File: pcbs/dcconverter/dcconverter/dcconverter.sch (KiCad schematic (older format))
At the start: 22 parts, among them IC1 NCP7805TG, J1 190-9991, J2 897-0711, J3 146-8335, Q1 124-8981, Q2 FQP47P06, Q3 2SK3747-1E

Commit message: Finish Schematic for PCB
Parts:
- removed Q3: 2SK3747-1E, TO545P570X1550X2990-3P, symbol SamacSys_Parts:2SK3747-1E
- added C4: 711-2096, Capacitor_THT:C_Disc_D7.5mm_W5.0mm_P7.50mm, symbol Device:C
- added D3, D4: 800-8872, Diode_THT:D_DO-41_SOD81_P10.16mm_Horizontal, symbol Device:D_Zener
- added HS-IC1: 893-4942, Heatsink:Heatsink_Fischer_SK129-STS_42x25mm_2xDrill2.5mm, symbol Mechanical:Heatsink_Pad_2Pin
- added Q10, Q5, Q6: 398-433, Package_TO_SOT_THT:TO-92_Inline, symbol Transistor_BJT:2N2219
- added Q3, Q4: 2SK3747-1E, Package_TO_SOT_THT:TO-3P-3_Horizontal_TabDown, symbol Transistor_FET:2N7000
- added Q7: 671-5118, Package_TO_SOT_THT:TO-220-3_Horizontal_TabDown, symbol Transistor_FET:AO3401A
- added Q8: 671-4809, Package_TO_SOT_THT:TO-3P-3_Horizontal_TabDown, symbol Transistor_FET:2N7000
- added R10: 10k, Resistor_THT:R_Axial_DIN0207_L6.3mm_D2.5mm_P10.16mm_Horizontal, symbol Device:R
- added R11, R7, R8: 220, Resistor_THT:R_Axial_DIN0207_L6.3mm_D2.5mm_P10.16mm_Horizontal, symbol Device:R
- added R5: 10M, Resistor_THT:R_Axial_DIN0207_L6.3mm_D2.5mm_P10.16mm_Horizontal, symbol Device:R
- added R6: 707-8546, Resistor_THT:R_Axial_DIN0207_L6.3mm_D2.5mm_P10.16mm_Horizontal, symbol Device:R
- added R9: 1k, Resistor_THT:R_Axial_DIN0207_L6.3mm_D2.5mm_P10.16mm_Horizontal, symbol Device:R
- IC1: footprint TO254P482X997X2018-3P -> Package_TO_SOT_THT:TO-220-3_Vertical
- J2: value 897-0711 -> 766-6629; footprint TerminalBlock_Altech:Altech_AK300_1x06_P5.00mm_45-Degree -> SamacSys_Parts:CES-106-XX-Y-S
- Q1: value 124-8981 -> NGTB40N120FL2WG
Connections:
- net at C1.2, C2.2, C3.2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: now also C4.2, D4.2 (A), Q10.1 (E), Q6.1 (E), Q8.1 (S)
- net at F1.1, Q1.1 (C), R3.1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: now also R5.1, R6.1
- net at Q1.3 (G): now also Q7.3 (D), Q8.3 (D)
- net at C2.1, R1.2, R2.1: now also J2.3 (Pin_3); no longer J2.2 (Pin_2)
- net at IC1.3 (OUTPUT): now also J2.2 (Pin_2); no longer J2.3 (Pin_3)
- net at J2.4 (Pin_4): now also R7.2
- net at J2.5 (Pin_5): now also R8.2
- net at J2.6 (Pin_6): now also R11.2
- net at D2.1 (K), R3.2: now also Q3.2 (G)
- net at R4.2: now also Q3.3 (D)
- net at C3.1, IC1.1 (INPUT): now also Q3.1 (S), R10.1
- net at Q2.1: now also Q10.3 (C), R10.2
- new net: D3.1 (K), Q4.2 (G), R5.2
- new net: Q4.3 (D), R6.2
- new net: D3.2 (A), D4.1 (K)
- new net: C4.1, Q4.1 (S), Q7.2 (S), R9.1
- new net: Q5.2 (B), R7.1
- new net: Q6.2 (B), R8.1
- new net: Q5.1 (E), Q6.3 (C)
- new net: Q5.3 (C), Q7.1 (G), Q8.2 (G), R9.2
- new net: Q10.2 (B), R11.1

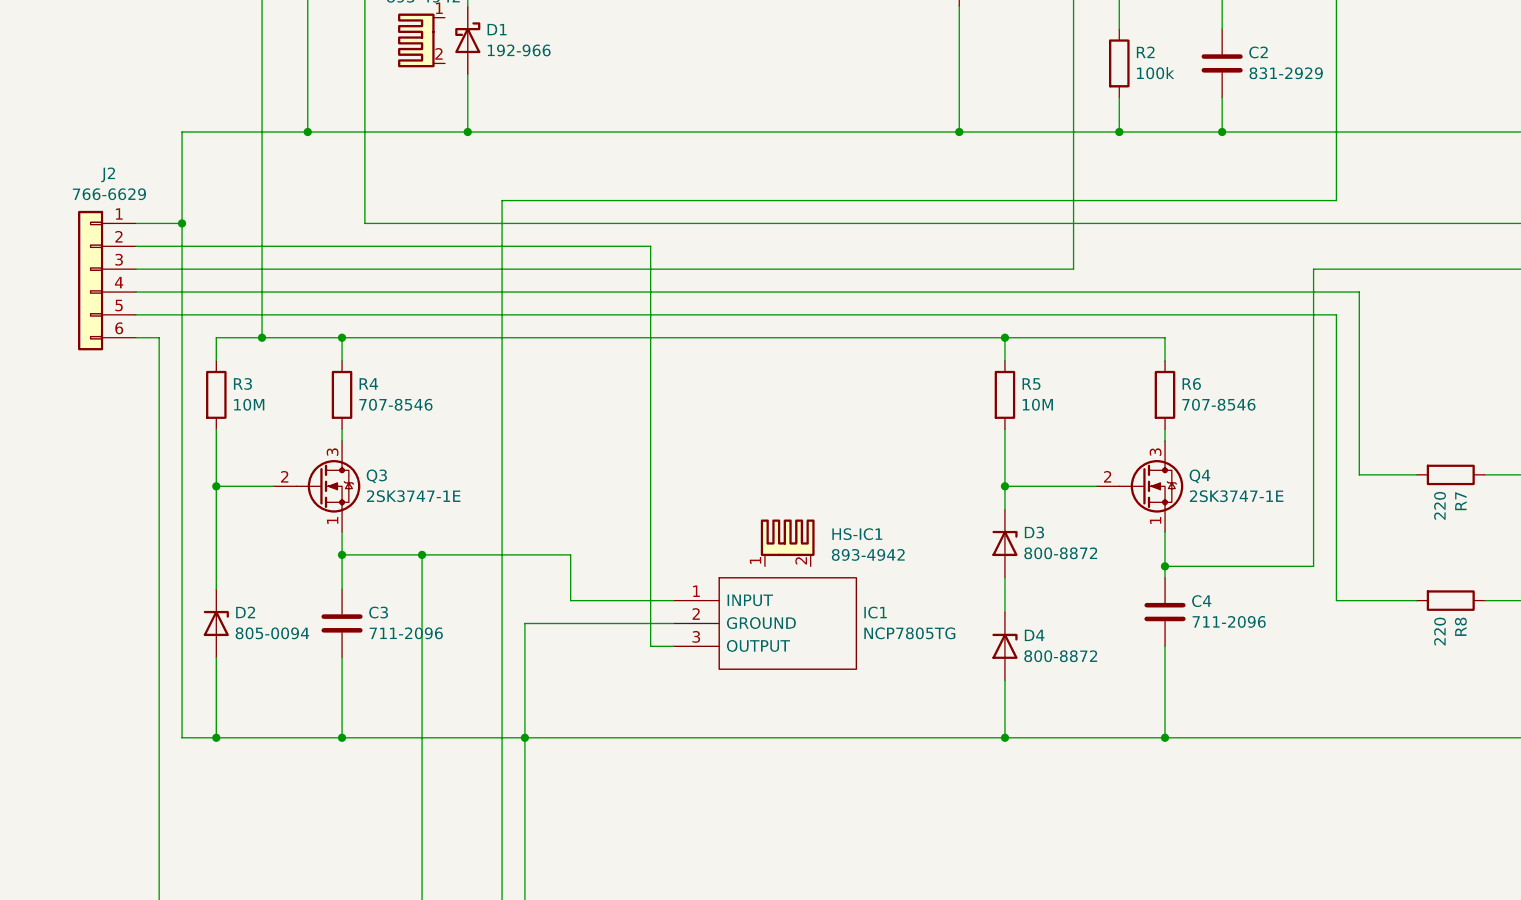
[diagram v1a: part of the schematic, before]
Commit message: Start with routing of DC Converter
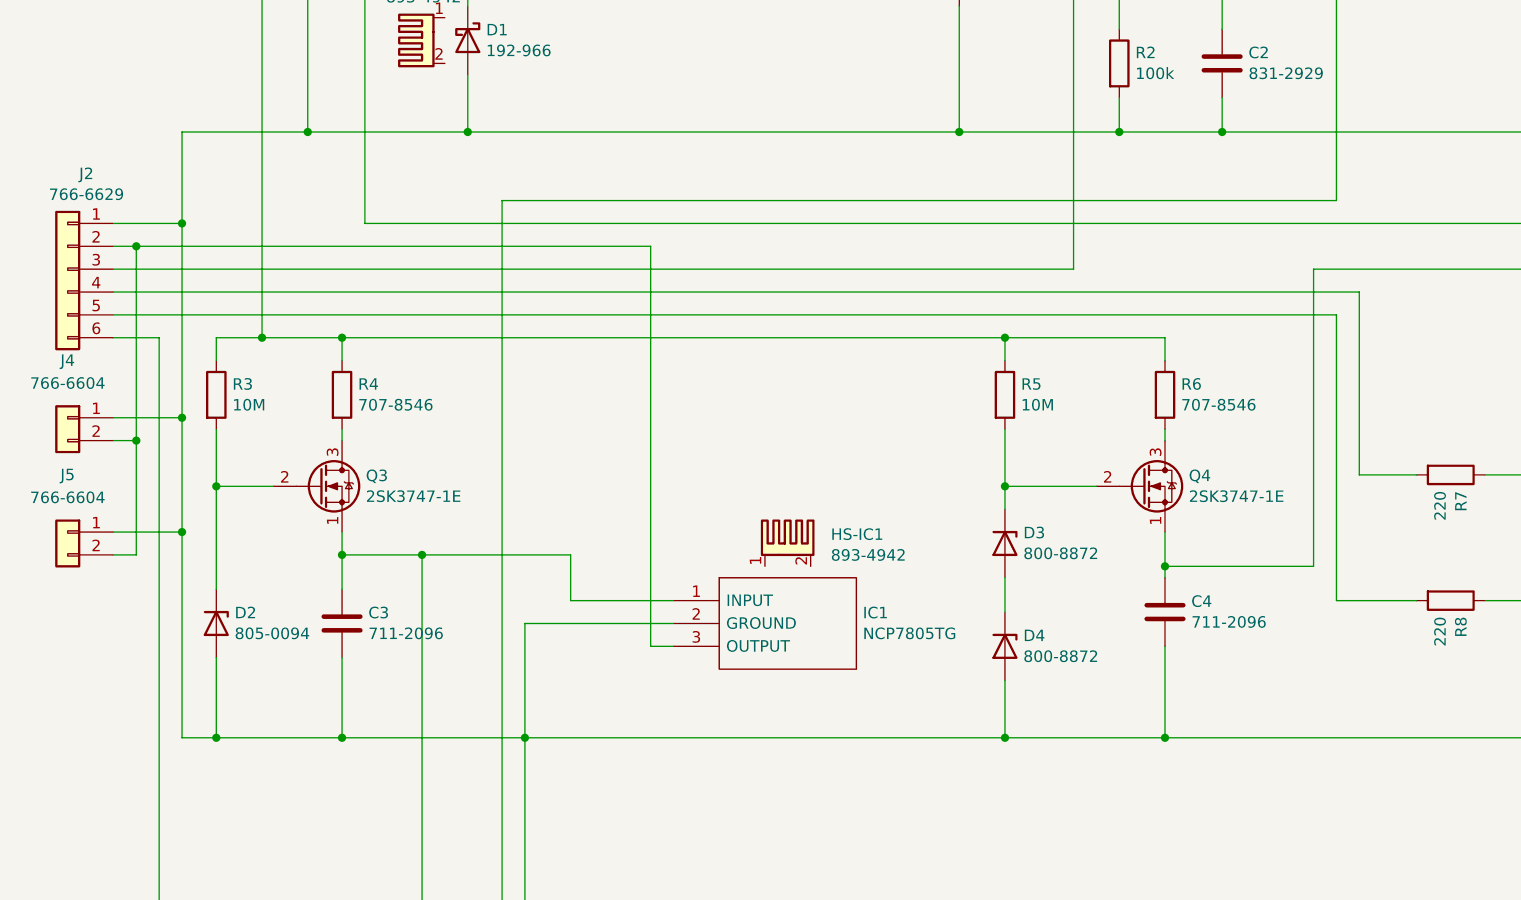
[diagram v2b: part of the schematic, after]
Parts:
- added J4, J5: 766-6604, SamacSys_Parts:CES-102-XX-Y-S, symbol Connector_Generic:Conn_01x02
- C3, C4: footprint Capacitor_THT:C_Disc_D7.5mm_W5.0mm_P7.50mm -> Capacitor_THT:CP_Radial_D18.0mm_P7.50mm
- Q8: footprint Package_TO_SOT_THT:TO-3P-3_Horizontal_TabDown -> Package_TO_SOT_THT:TO-220-3_Horizontal_TabDown
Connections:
- net at C1.2, C2.2, C3.2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: now also J4.1 (Pin_1), J5.1 (Pin_1)
- net at IC1.3 (OUTPUT), J2.2 (Pin_2): now also J4.2 (Pin_2), J5.2 (Pin_2)
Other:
- moved on the sheet: J2
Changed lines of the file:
@@
 L Connector_Generic:Conn_01x06 J2
 U 1 1 5F93B3A3
-P 1250 3700
-F 0 "J2" H 1168 4117 50  0000 C CNN
-F 1 "766-6629" H 1168 4026 50  0000 C CNN
-F 2 "SamacSys_Parts:CES-106-XX-Y-S" H 1250 3700 50  0001 C CNN
-F 3 "~" H 1250 3700 50  0001 C CNN
-	1    1250 3700
+P 1150 3700
+F 0 "J2" H 1068 4117 50  0000 C CNN
+F 1 "766-6629" H 1068 4026 50  0000 C CNN
+F 2 "SamacSys_Parts:CES-106-XX-Y-S" H 1150 3700 50  0001 C CNN
+F 3 "~" H 1150 3700 50  0001 C CNN
+	1    1150 3700
 	-1   0    0    -1
 $EndComp
@@
 F 0 "C3" H 2465 5296 50  0000 L CNN
 F 1 "711-2096" H 2465 5205 50  0000 L CNN
-F 2 "Capacitor_THT:C_Disc_D7.5mm_W5.0mm_P7.50mm" H 2388 5100 50  0001 C CNN
+F 2 "Capacitor_THT:CP_Radial_D18.0mm_P7.50mm" H 2388 5100 50  0001 C CNN
 F 3 "~" H 2350 5250 50  0001 C CNN
 	1    2350 5250
@@
 F 0 "C4" H 6065 5246 50  0000 L CNN
 F 1 "711-2096" H 6065 5155 50  0000 L CNN
-F 2 "Capacitor_THT:C_Disc_D7.5mm_W5.0mm_P7.50mm" H 5988 5050 50  0001 C CNN
+F 2 "Capacitor_THT:CP_Radial_D18.0mm_P7.50mm" H 5988 5050 50  0001 C CNN
 F 3 "~" H 5950 5200 50  0001 C CNN
 	1    5950 5200
@@
 	7850 4800 7850 4950
 Wire Wire Line
-	1450 3800 6800 3800
-Wire Wire Line
 	6800 3800 6800 4600
 Wire Wire Line
@@
 Wire Wire Line
 	6700 5150 6700 3900
-Wire Wire Line
-	6700 3900 1450 3900
 $Comp
 L Device:R R9
@@
 F 0 "Q8" H 9404 5096 50  0000 L CNN
 F 1 "671-4809" H 9404 5005 50  0000 L CNN
-F 2 "Package_TO_SOT_THT:TO-3P-3_Horizontal_TabDown" H 9400 4975 50  0001 L CIN
+F 2 "Package_TO_SOT_THT:TO-220-3_Horizontal_TabDown" H 9400 4975 50  0001 L CIN
 F 3 "" H 9200 5050 50  0001 L CNN
 	1    9200 5050
@@
 	1550 7300 1550 4000
 Wire Wire Line
-	1550 4000 1450 4000
-Wire Wire Line
 	6700 2250 6700 3400
 Wire Wire Line
@@
 Wire Wire Line
 	2700 6950 2700 6800
-Wire Wire Line
-	1450 3500 1650 3500
 Connection ~ 1650 3500
 Wire Wire Line
-	1650 3500 1650 5750
-Wire Wire Line
-	3700 3600 1450 3600
+	1650 3500 1650 4350
 Wire Wire Line
 	3700 3600 3700 5350
 Wire Wire Line
-	1450 3700 5550 3700
-Wire Wire Line
 	5550 2500 5550 3700
+$Comp
+L Connector_Generic:Conn_01x02 J4
+U 1 1 5FA3A804
+P 1150 4350
+F 0 "J4" H 1150 4600 50  0000 C CNN
+F 1 "766-6604" H 1150 4500 50  0000 C CNN
+F 2 "SamacSys_Parts:CES-102-XX-Y-S" H 1150 4350 50  0001 C CNN
+F 3 "~" H 1150 4350 50  0001 C CNN
+	1    1150 4350
+	-1   0    0    -1
+$EndComp
+Wire Wire Line
+	1350 3500 1650 3500
+Wire Wire Line
+	1350 3600 1450 3600
+Wire Wire Line
+	1350 3700 5550 3700
+Wire Wire Line
+	1350 3800 6800 3800
+Wire Wire Line
+	1350 3900 6700 3900
+Wire Wire Line
+	1350 4000 1550 4000
+$Comp
+L Connector_Generic:Conn_01x02 J5
+U 1 1 5FA5AA03
+P 1150 4850
+F 0 "J5" H 1150 5100 50  0000 C CNN
+F 1 "766-6604" H 1150 5000 50  0000 C CNN
+F 2 "SamacSys_Parts:CES-102-XX-Y-S" H 1150 4850 50  0001 C CNN
+F 3 "~" H 1150 4850 50  0001 C CNN
+	1    1150 4850
+	-1   0    0    -1
+$EndComp
+Wire Wire Line
+	1650 4350 1350 4350
+Connection ~ 1650 4350
+Wire Wire Line
+	1650 4350 1650 4850
+Wire Wire Line
+	1650 4850 1350 4850
+Connection ~ 1650 4850
+Wire Wire Line
+	1650 4850 1650 5750
+Wire Wire Line
+	1450 3600 1450 4450
+Wire Wire Line
+	1450 4450 1350 4450
+Connection ~ 1450 3600
+Wire Wire Line
+	1450 3600 3700 3600
+Wire Wire Line
+	1350 4950 1450 4950
+Wire Wire Line
+	1450 4950 1450 4450
+Connection ~ 1450 4450
 $EndSCHEMATC
